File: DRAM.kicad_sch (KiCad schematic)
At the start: 1 part, among them U3 MT41K256M16TW

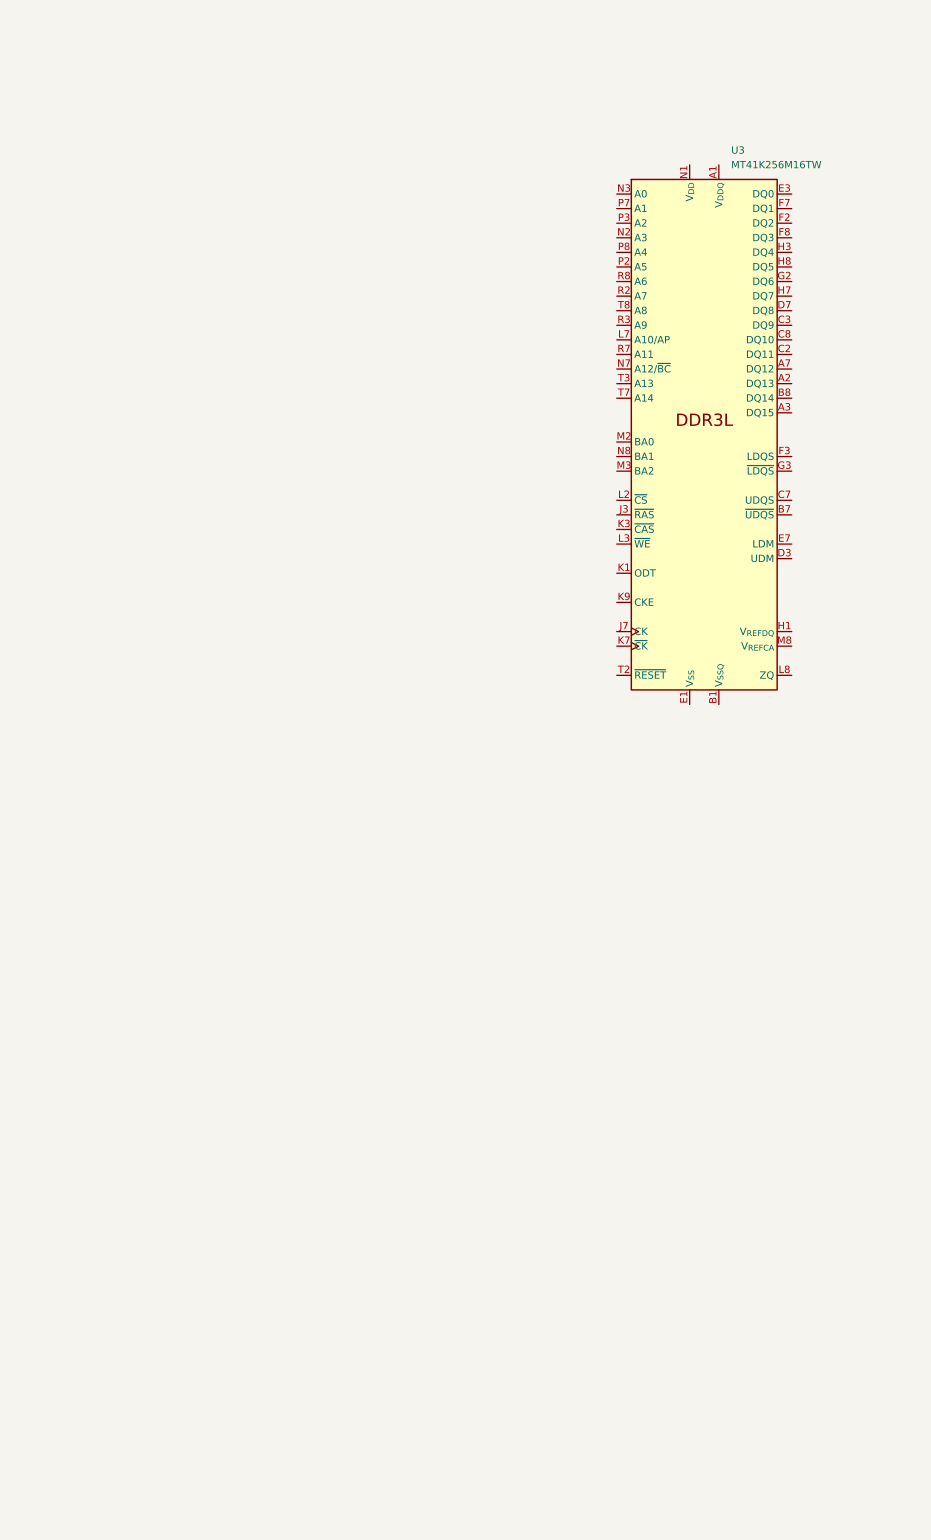
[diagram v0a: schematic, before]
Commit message: Changed power regulators, filled out DRAM, begin changing FPGA from ECP5 to ICE40
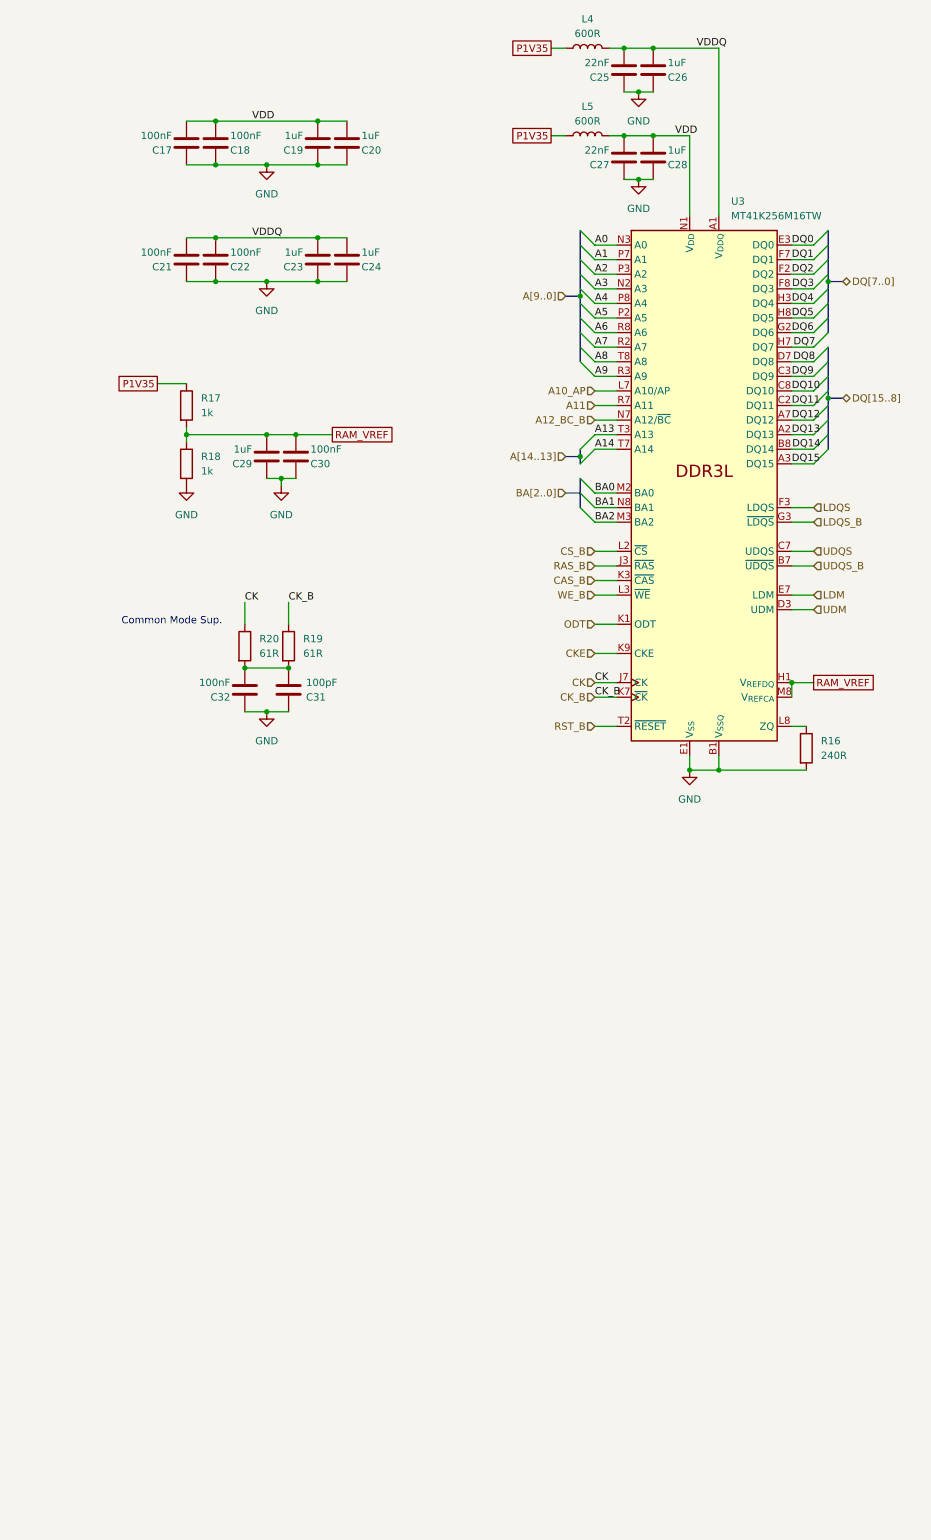
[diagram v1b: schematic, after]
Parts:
- added C17, C18, C21, C22, C30, C32: 100nF, symbol Device:C
- added C19, C20, C23, C24, C26, C28, C29: 1uF, symbol Device:C
- added C25, C27: 22nF, symbol Device:C
- added C31: 100pF, symbol Device:C
- added L4, L5: 600R, symbol Device:L
- added R16: 240R, symbol Device:R
- added R17, R18: 1k, symbol Device:R
- added R19, R20: 61R, symbol Device:R
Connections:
- net VDDQ: now reaches U3.A1 (V_{DDQ}), U3.A8 (V_{DDQ}), U3.C1 (V_{DDQ}), U3.C9 (V_{DDQ}), U3.D2 (V_{DDQ}), U3.E9 (V_{DDQ}), U3.F1 (V_{DDQ}), U3.H2 (V_{DDQ}), U3.H9 (V_{DDQ})
- net VDDQ: now also C21.1, C22.1, C23.1, C24.1, C25.1, C26.1, L4.2
- net DQ13: now reaches U3.A2 (DQ13)
- net DQ15: now reaches U3.A3 (DQ15)
- net DQ12: now reaches U3.A7 (DQ12)
- net GND: now reaches U3.A9 (V_{SS}), U3.B3 (V_{SS}), U3.E1 (V_{SS}), U3.G8 (V_{SS}), U3.J2 (V_{SS}), U3.J8 (V_{SS}), U3.M1 (V_{SS}), U3.M9 (V_{SS}), U3.P1 (V_{SS}), U3.P9 (V_{SS}), U3.T1 (V_{SS}), U3.T9 (V_{SS})
- net GND: now also U3.B1 (V_{SSQ}), U3.B9 (V_{SSQ}), U3.D1 (V_{SSQ}), U3.D8 (V_{SSQ}), U3.E2 (V_{SSQ}), U3.E8 (V_{SSQ}), U3.F9 (V_{SSQ}), U3.G1 (V_{SSQ}), U3.G9 (V_{SSQ}), C17.2, C18.2, C19.2, C20.2, C21.2, C22.2, C23.2, C24.2, C25.2, C26.2, C27.2, C28.2, C29.2, C30.2, C31.2, C32.2, R16.2, R18.2
- net VDD: now reaches U3.B2 (V_{DD}), U3.D9 (V_{DD}), U3.G7 (V_{DD}), U3.K2 (V_{DD}), U3.K8 (V_{DD}), U3.N1 (V_{DD}), U3.N9 (V_{DD}), U3.R1 (V_{DD}), U3.R9 (V_{DD})
- net VDD: now also C17.1, C18.1, C19.1, C20.1, C27.1, C28.1, L5.2
- net UDQS_B: now reaches U3.B7 (~{UDQS})
- net DQ14: now reaches U3.B8 (DQ14)
- net DQ11: now reaches U3.C2 (DQ11)
- net DQ9: now reaches U3.C3 (DQ9)
- net UDQS: now reaches U3.C7 (UDQS)
- net DQ10: now reaches U3.C8 (DQ10)
- net UDM: now reaches U3.D3 (UDM)
- net DQ8: now reaches U3.D7 (DQ8)
- net DQ0: now reaches U3.E3 (DQ0)
- net LDM: now reaches U3.E7 (LDM)
- net DQ2: now reaches U3.F2 (DQ2)
- net LDQS: now reaches U3.F3 (LDQS)
- net DQ1: now reaches U3.F7 (DQ1)
- net DQ3: now reaches U3.F8 (DQ3)
- net DQ6: now reaches U3.G2 (DQ6)
- net LDQS_B: now reaches U3.G3 (~{LDQS})
- net RAM_VREF: now reaches U3.H1 (V_{REFDQ})
- net RAM_VREF: now also U3.M8 (V_{REFCA}), C29.1, C30.1, R17.2, R18.1
- net DQ4: now reaches U3.H3 (DQ4)
- net DQ7: now reaches U3.H7 (DQ7)
- net DQ5: now reaches U3.H8 (DQ5)
- net RAS_B: now reaches U3.J3 (~{RAS})
- net CK: now reaches U3.J7 (CK)
- net CK: now also R20.1
- net ODT: now reaches U3.K1 (ODT)
- net CAS_B: now reaches U3.K3 (~{CAS})
- net CK_B: now reaches U3.K7 (~{CK})
- net CK_B: now also R19.1
- net CKE: now reaches U3.K9 (CKE)
- net CS_B: now reaches U3.L2 (~{CS})
- net WE_B: now reaches U3.L3 (~{WE})
- net A10_AP: now reaches U3.L7 (A10/AP)
- net at U3.L8 (ZQ): now also R16.1
- net BA0: now reaches U3.M2 (BA0)
- net BA2: now reaches U3.M3 (BA2)
- net A3: now reaches U3.N2 (A3)
- net A0: now reaches U3.N3 (A0)
- net A12_BC_B: now reaches U3.N7 (A12/~{BC})
- net BA1: now reaches U3.N8 (BA1)
- net A5: now reaches U3.P2 (A5)
- net A2: now reaches U3.P3 (A2)
- net A1: now reaches U3.P7 (A1)
- net A4: now reaches U3.P8 (A4)
- net A7: now reaches U3.R2 (A7)
- net A9: now reaches U3.R3 (A9)
- net A11: now reaches U3.R7 (A11)
- net A6: now reaches U3.R8 (A6)
- net RST_B: now reaches U3.T2 (~{RESET})
- net A13: now reaches U3.T3 (A13)
- net A14: now reaches U3.T7 (A14)
- net A8: now reaches U3.T8 (A8)
- new net: C31.1, C32.1, R19.2, R20.2
- new net P1V35: L4.1, L5.1, R17.1
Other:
- note added: "Common Mode Sup."
- moved on the sheet: U3

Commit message: Saving before changing RAM from DDR3 to Parallel SDR SRAM
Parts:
- added U6: AS6C1616, Package_SO:TSOP-I-48_18.4x12mm_P0.5mm, symbol Memory_RAM:AS6C1616
- renumbered C17 to C15, C21 to C16, C18 to C33, C22 to C34, C32 to C35, C29 to C36, C31 to C37, C30 to C38, C19 to C39, C23 to C40, C20 to C41, C24 to C42, C25 to C43, C27 to C44, C26 to C45, C28 to C46, L4 to L7, L5 to L8, R17 to R23, R18 to R24, R20 to R25, R19 to R26, R16 to R27, U3 to U7
